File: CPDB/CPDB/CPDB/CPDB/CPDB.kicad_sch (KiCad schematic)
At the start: 26 parts, among them J1 Conn_01x02_Pin, J2 Conn_01x04_Pin, U1 INA219BxDCN, U2 TPS54302DDCR, U3 TPS563240DDCR

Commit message: gruplama yapıldı, indüktörler değişti
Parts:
- L1: footprint Inductor_SMD:L_Chilisin_BMRF00131350 -> Inductor_SMD:L_Sunlord_SWPA6045S
- L2: footprint Inductor_SMD:L_Bourns-SRN8040_8x8.15mm -> Inductor_SMD:L_Coilcraft_XAL4020-XXX
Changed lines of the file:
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@@
 			)
 		)
-		(property "Footprint" "Inductor_SMD:L_Bourns-SRN8040_8x8.15mm"
+		(property "Footprint" "Inductor_SMD:L_Coilcraft_XAL4020-XXX"
 			(at 129.54 121.92 0)
 			(effects
@@
 			)
 		)
-		(property "Footprint" "Inductor_SMD:L_Chilisin_BMRF00131350"
+		(property "Footprint" "Inductor_SMD:L_Sunlord_SWPA6045S"
 			(at 119.38 48.26 0)
 			(effects

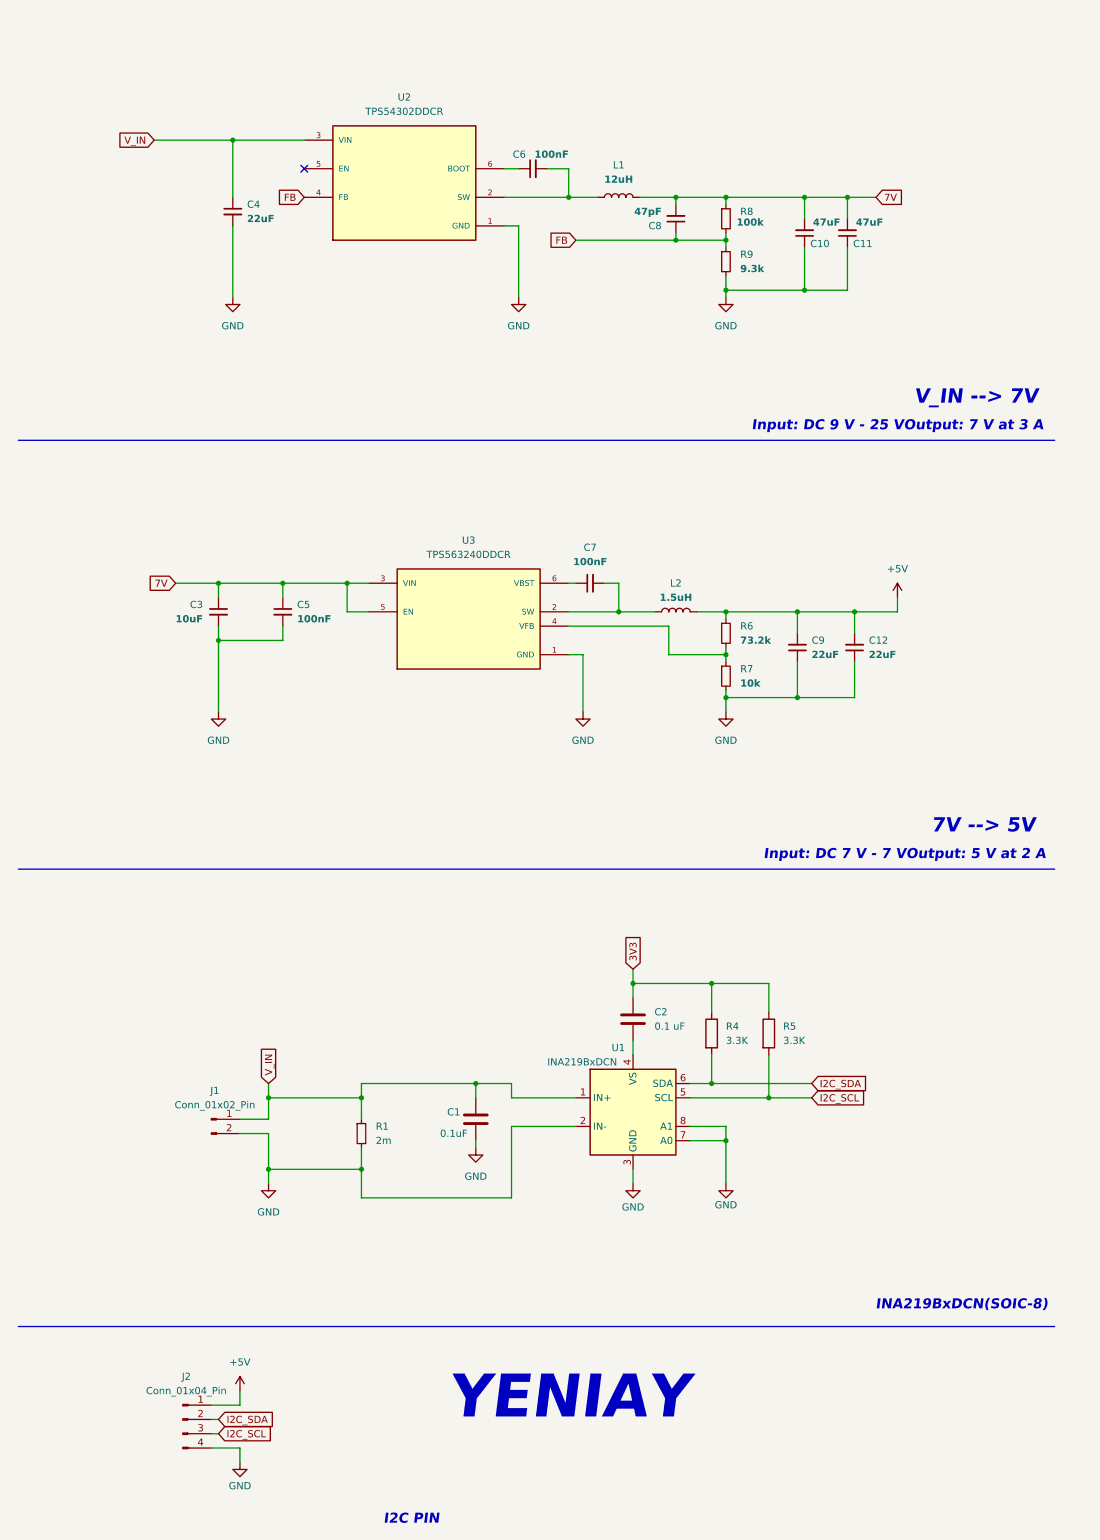
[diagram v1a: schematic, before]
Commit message: ESC pin placement.
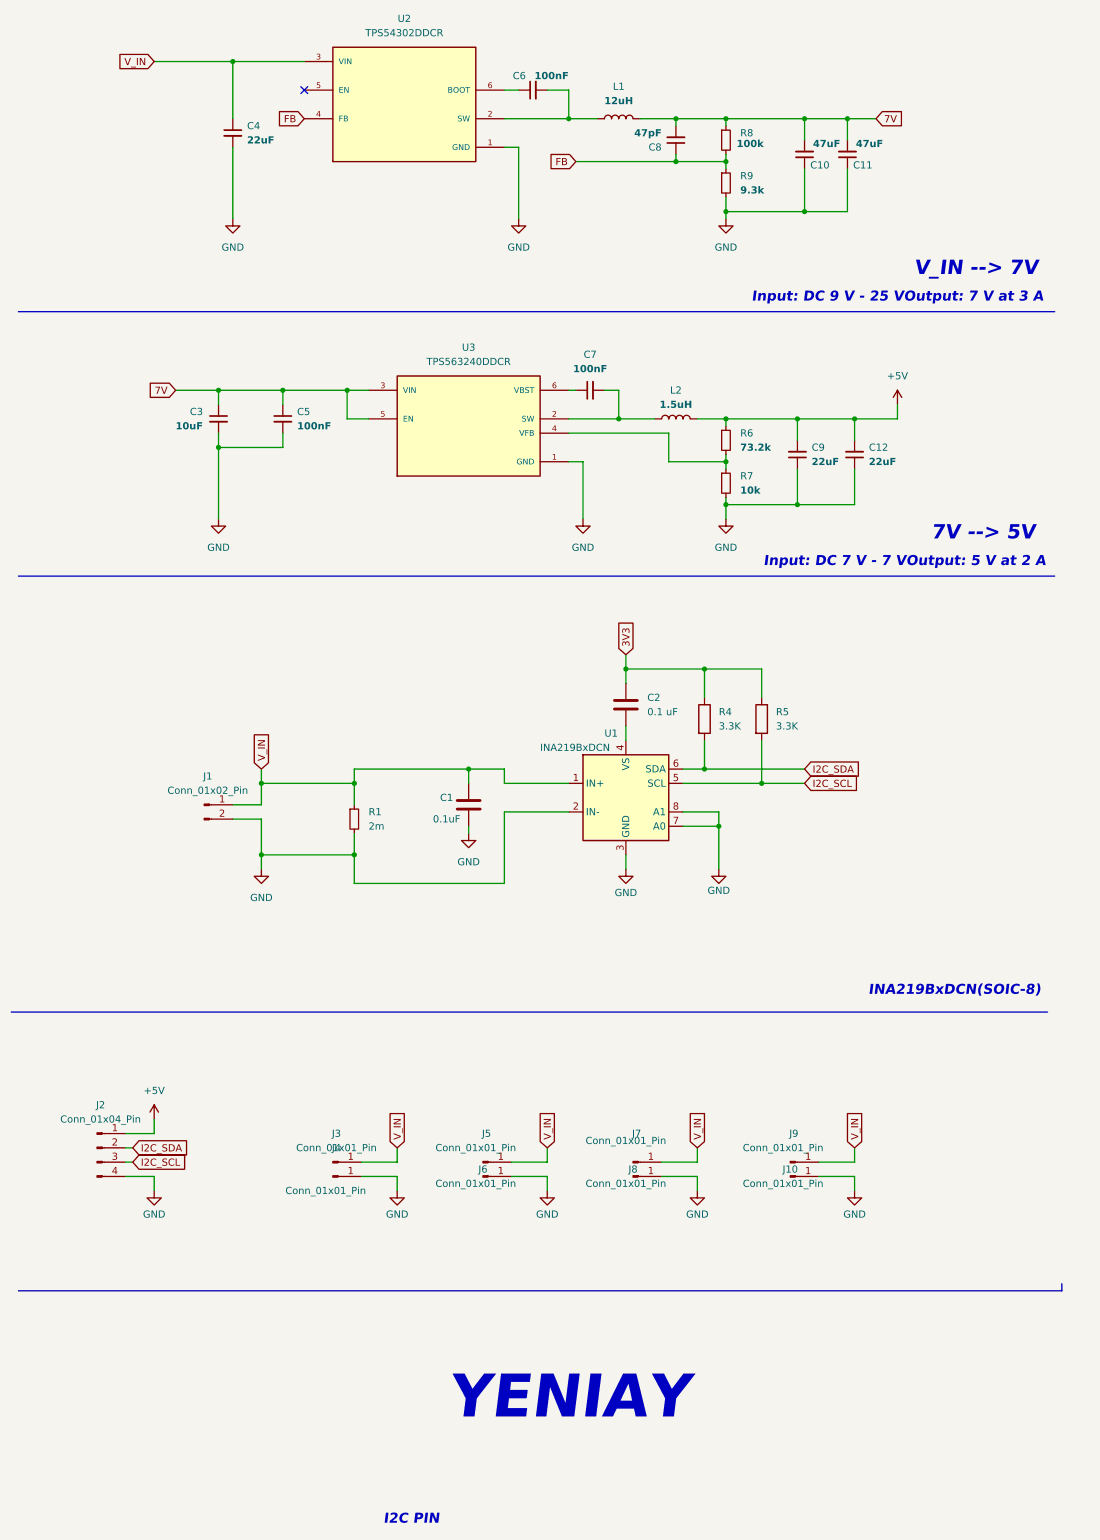
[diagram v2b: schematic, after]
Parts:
- added J10, J3, J4, J5, J6, J7, J8, J9: Conn_01x01_Pin, Connector_Samtec_HPM_THT:Samtec_HPM-01-05-x-S_Straight_1x01_Pitch5.08mm, symbol Connector:Conn_01x01_Pin
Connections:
- net GND: now also J10.1 (Pin_1), J4.1 (Pin_1), J6.1 (Pin_1), J8.1 (Pin_1)
- net V_IN: now also J3.1 (Pin_1), J5.1 (Pin_1), J7.1 (Pin_1), J9.1 (Pin_1)
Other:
- moved on the sheet: C1, C10, C11, C12, C2, C3, C4, C5, C6, C7, C8, C9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
